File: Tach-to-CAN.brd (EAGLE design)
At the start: 38 x 34.5 mm, 51 parts, among them J1 CONN_4PIN_VERT, J2 CONN_4PIN_VERT, Q1 NXP_NX3008NBK,215NXP_SOT23, Q2 8MHz, U1 VISHAY_VOMA618A-2X001T, U3 TI_TPS7A1633AQDGNRQ1, U4 STM32F303K8T6STMICROELECTRONI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

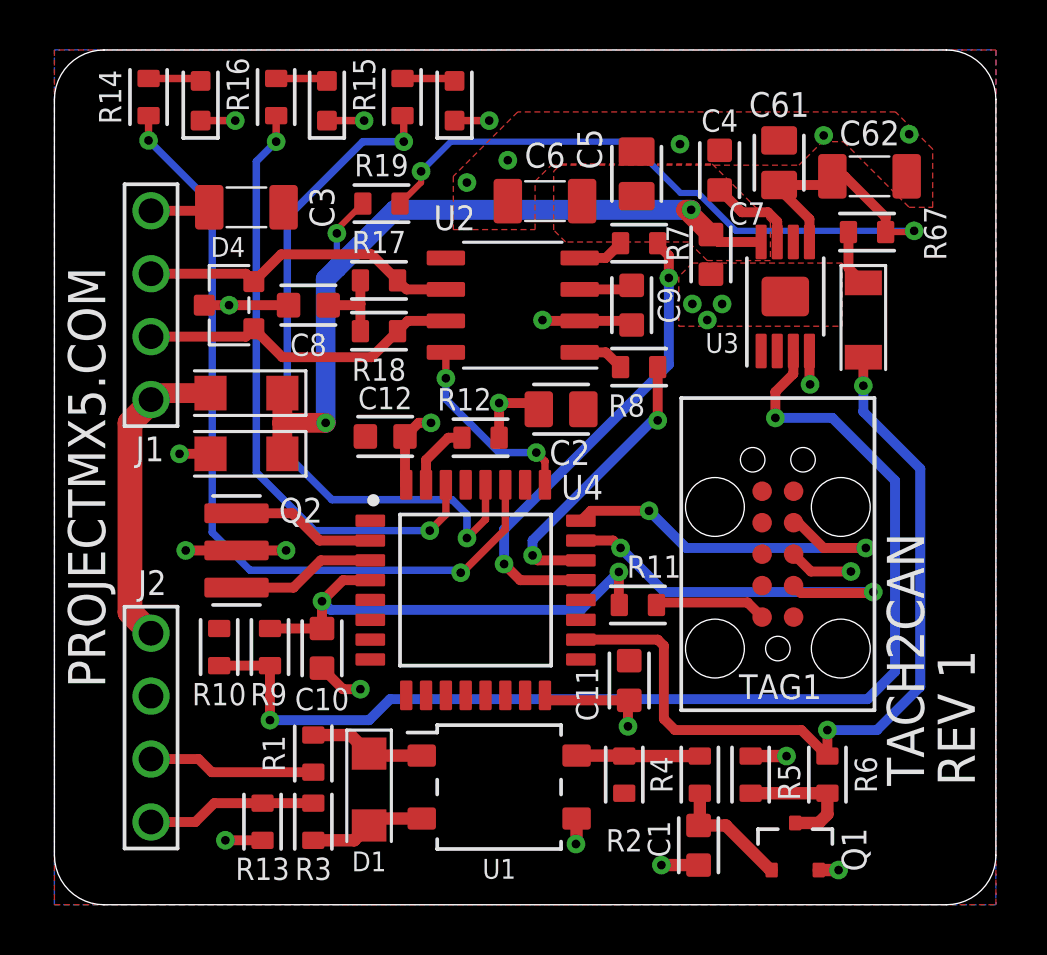
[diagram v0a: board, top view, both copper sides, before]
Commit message: Add NFET to buffer TACH_IN signal
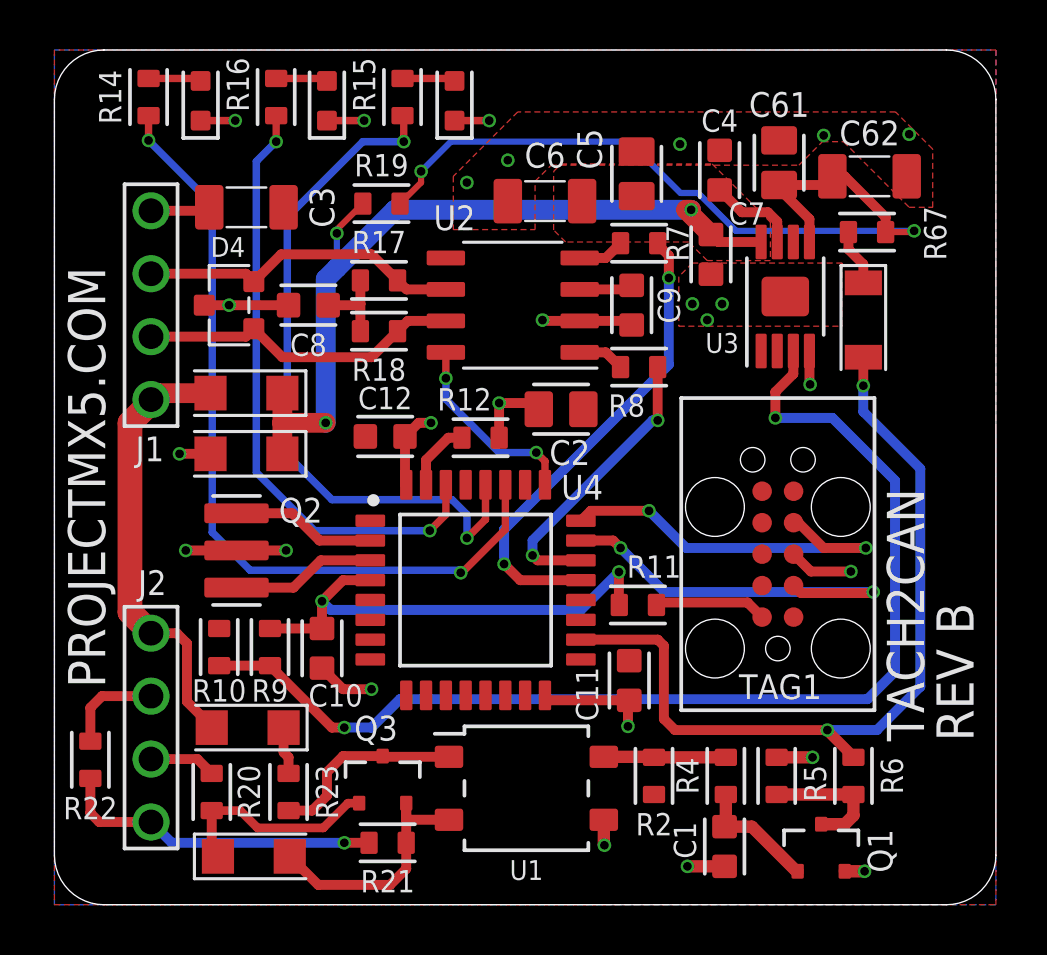
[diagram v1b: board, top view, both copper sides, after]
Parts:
- removed R1, R3: 1k, resistors:REST-0603
- removed R13: 0, resistors:REST-0603
- added D9: VISHAY_SMF18A-HM3-08, AlphaLibrary:VISHAY_SMFXXA-HM3-08
- added Q3: NEXPERIA_PMV60ENEAR, AlphaLibrary:NXP_SOT23
- added R20, R21, R23: 1k, resistors:REST-0603
- added R22: 0, resistors:REST-0603
- U2: value (none) -> TI_SN65HVD23X
- moved D1 5.50 mm to (7.80, 7.15), turned to 0 degrees
- moved R2 1.20 mm to (24.2, 5.20)
- moved U1 1.10 mm to (19.1, 4.70)
- moved C1 1.05 mm to (27.1, 2.35)
- moved Q1 1.05 mm to (30.9, 2.30)
- moved R4 1.05 mm to (27.1, 5.20)
- moved R6 1.05 mm to (32.2, 5.20)
- moved R5 1.05 mm to (29.1, 5.20)
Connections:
- new net PWR_RAW_PU: D1.C, R23.1
- new net TACH_IN_N: Q3.3, R23.2, U1.1
- net GND: now also R22.1; no longer R13.1
- net PWR_RAW: now also D1.A
- net TACH_ANODE: now also D9.C, Q3.1, R20.2; no longer D1.C, R1.2, U1.1
- net TACH_GND: now also R21.1, R22.2; no longer R13.2, R3.1
- net TACH_GND_R: now also D9.A, Q3.2, R21.2; no longer D1.A, R3.2
- net TACH_IN\: now also R20.1; no longer R1.1
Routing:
- net TACH_IN_N: track 0.00 -> 7.96 mm
- net TACH_GND: track 6.86 -> 13.1 mm, vias 0 -> 1
- net TACH_GND_R: track 4.74 -> 10.5 mm
- net PWR_RAW: track 12.6 -> 18.1 mm
- net TACH_IN\: track 6.77 -> 2.69 mm
- net TACH_ANODE: track 4.72 -> 8.61 mm
- net GND: track 40.9 -> 43.8 mm, vias 26 -> 25
- net PWR_RAW_PU: track 0.00 -> 1.93 mm
- net RPM: track 33.4 -> 35.0 mm
- net MCU_EN: track 46.9 -> 45.8 mm
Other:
- board text added: "REV B"
- board text removed: "REV 1"
